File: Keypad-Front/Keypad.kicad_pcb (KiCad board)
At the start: 4 copper layers, 100.1 x 192.1 mm, 62 parts, among them J1 RTC STEMMA QT, J10 EXP QWIIC, J11 TOUCH QWIIC, J6 JST-PH 6, J7 JST-PH 6, J8 Feedback, U1 DS3231MZ, U2 LM1117-3.3, U3 CAP1214

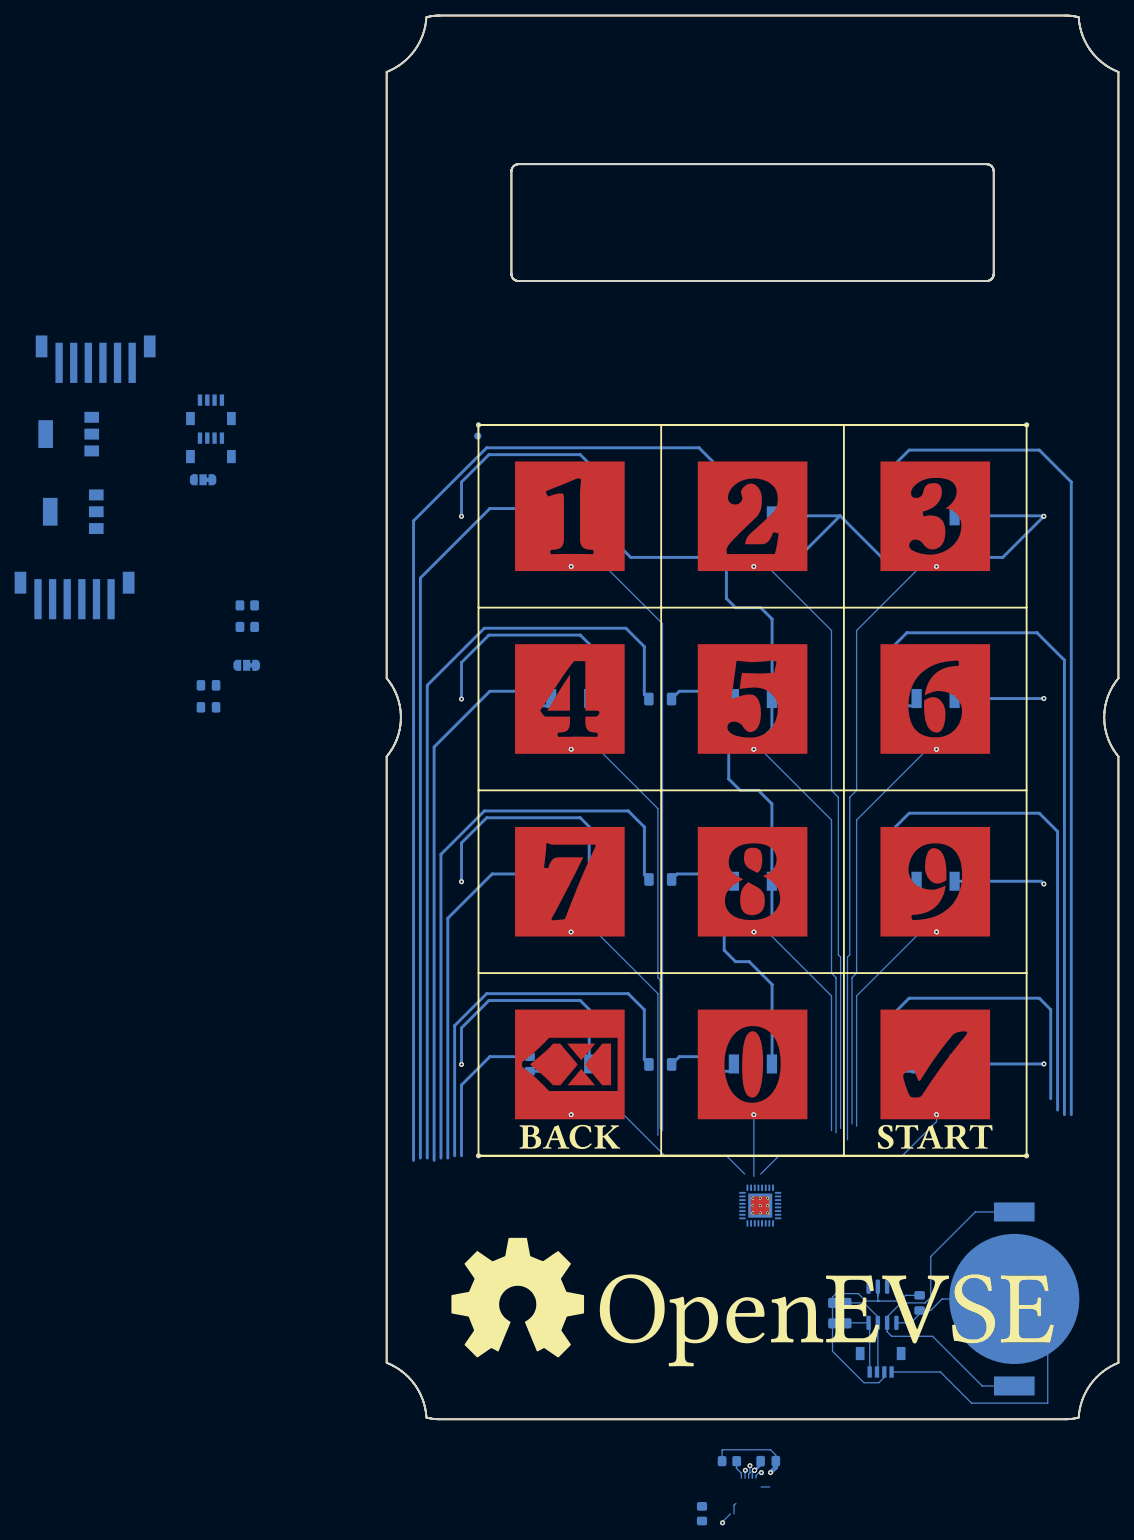
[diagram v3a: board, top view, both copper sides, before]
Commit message: Take 3, the JST-XH for the feedback is too large.
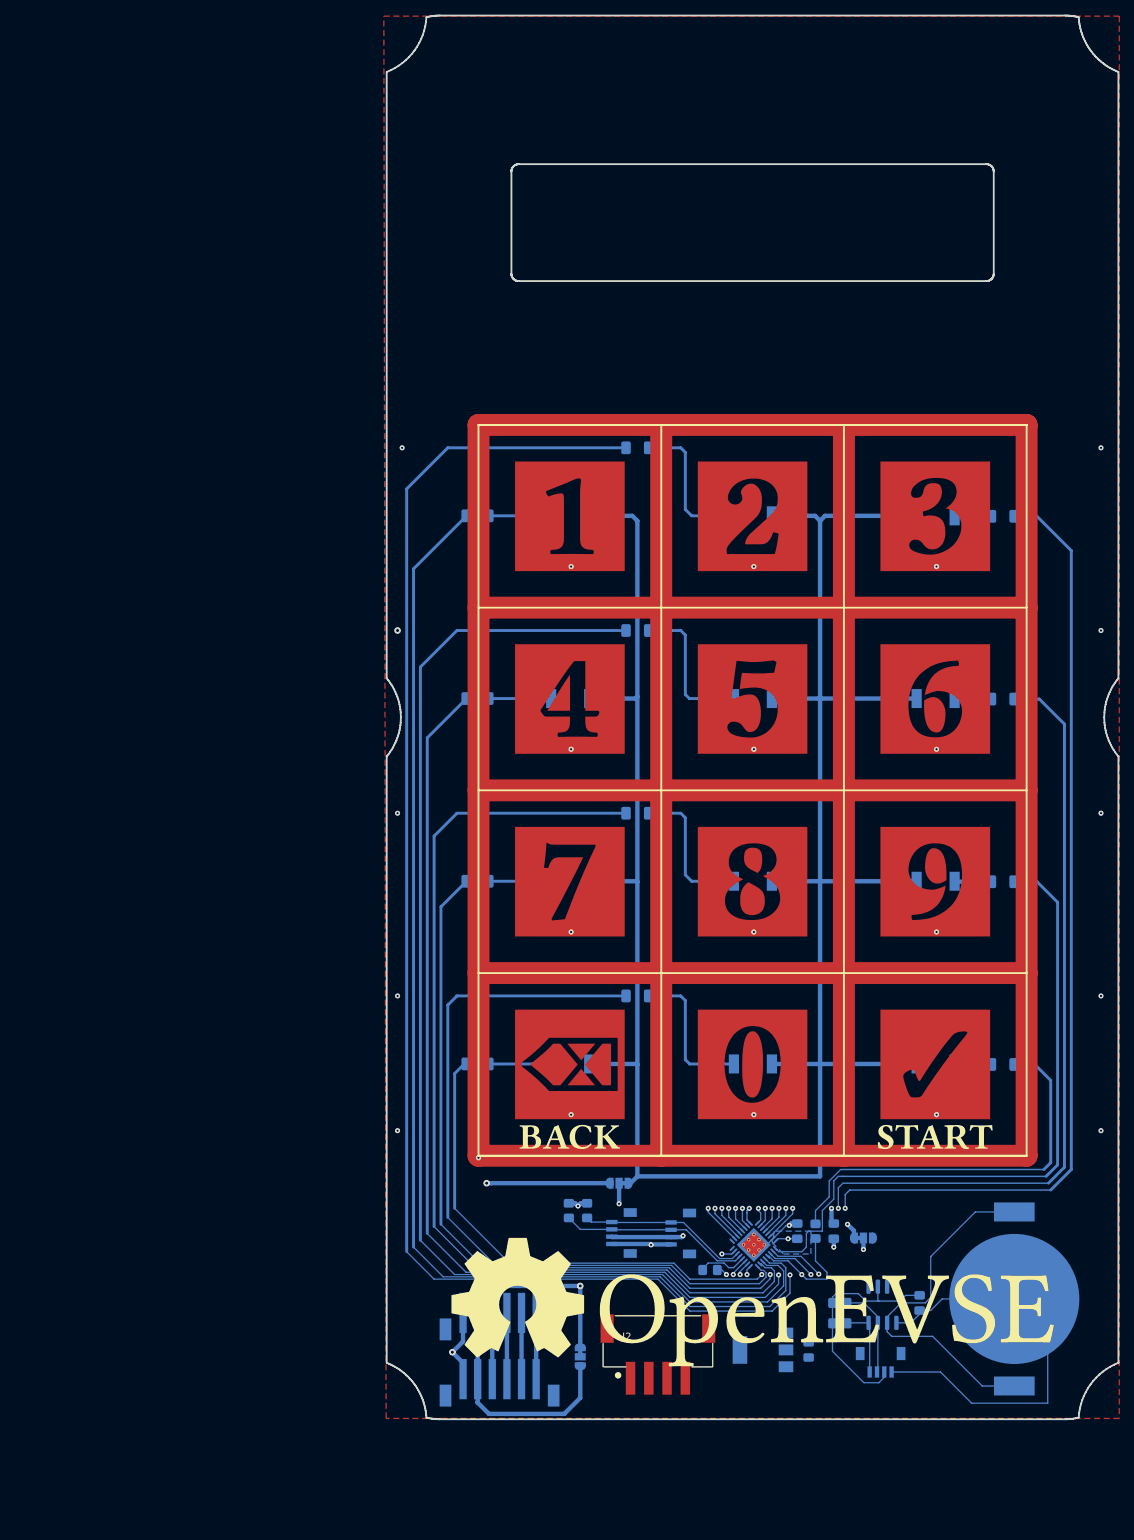
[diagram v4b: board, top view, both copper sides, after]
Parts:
- removed J8: Feedback, Package_TO_SOT_SMD:SOT-223-3_TabPin2
- removed R16, R20, R21: 0, Resistor_SMD:R_1206_3216Metric_Pad1.30x1.75mm_HandSolder
- added J2: JST-XH-4, Keypad:JST-XH-4-SMD, F.Cu at (91.2, 205.1)
- added JP3: PWR SEL, Jumper:SolderJumper-3_P1.3mm_Bridged12_RoundedPad1.0x1.5mm, B.Cu at (84.4, 202.2)
- R1, R10, R11, R12, R2, R3, R4, R5, R6, R7, R8, R9: footprint Resistor_SMD:R_0805_2012Metric_Pad1.20x1.40mm_HandSolder -> Resistor_SMD:R_1206_3216Metric_Pad1.30x1.75mm_HandSolder
- R17, R18: value 4.7k -> 10k
- TP14: moved to F.Cu
- moved U2 148.5 mm to (109.4, 201.2)
- moved J4 137.7 mm to (68.3, 196.2), turned to 0 degrees
- moved J6 130.3 mm to (96.8, 185.3), turned to -90 degrees
- moved J7 121.8 mm to (88.7, 185.3), turned to -90 degrees
- moved C3 120.3 mm to (115.6, 201.2), turned to 90 degrees
- moved J3 117.1 mm to (68.3, 205.2), turned to 0 degrees
- moved JP1 115.2 mm to (123.1, 185.9), turned to 0 degrees
- moved C2 113.6 mm to (119.1, 185.0), turned to 90 degrees
- moved JP2 111.8 mm to (89.7, 178.4)
- moved TP14 97.1 mm to (70.4, 173.3), turned to 0 degrees
- moved R17 95.0 mm to (85.3, 182.2), turned to -90 degrees
- moved R18 91.2 mm to (82.8, 182.2), turned to -90 degrees
- moved R15 41.7 mm to (116.6, 185.0)
- moved C4 31.7 mm to (114.1, 185.0), turned to 90 degrees
- moved R19 26.3 mm to (102.1, 190.3), turned to 0 degrees
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- renumbered J6 to J3, J7 to J4, J10 to J6, J11 to J7
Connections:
- net Net-(JP1-B) renamed /VREG
- R15 pad 1: /LED12 -> /LED10
- R15 pad 2: /LED10 -> /LED12
- R17 pad 2: Net-(U3-SMCLK) -> /TOUCH_SCL
- R18 pad 2: Net-(U3-SMDATA) -> /TOUCH_SDA
- U3 pad 1: /TOUCH_4 -> /TOUCH_11
- U3 pad 10: Net-(U3-LED2) -> /LED4
- U3 pad 11: /LED9 -> /LED7
- U3 pad 12: Net-(U3-LED4) -> /LED10
- U3 pad 13: /LED7 -> /LED1
- U3 pad 14: /LED6 -> /LED5
- U3 pad 15: Net-(U3-LED7) -> /LED8
- U3 pad 16: /LED4 -> /LED11
- U3 pad 17: /LED3 -> /LED2
- U3 pad 18: /LED2 -> /LED3
- U3 pad 19: /LED1 -> /LED6
- U3 pad 2: /TOUCH_3 -> /TOUCH_2
- U3 pad 21: Net-(U3-SMDATA) -> /TOUCH_SDA
- U3 pad 22: Net-(U3-SMCLK) -> /TOUCH_SCL
- U3 pad 27: /TOUCH_11 -> /TOUCH_4
- U3 pad 28: /TOUCH_9 -> /TOUCH_7
- U3 pad 29: /TOUCH_8 -> /TOUCH_10
- U3 pad 3: /TOUCH_2 -> /TOUCH_3
- U3 pad 30: /TOUCH_7 -> /TOUCH_1
- U3 pad 31: /TOUCH_6 -> /TOUCH_5
- U3 pad 32: /TOUCH_5 -> /TOUCH_8
- U3 pad 4: /TOUCH_1 -> /TOUCH_12
- U3 pad 5: /TOUCH_12 -> /TOUCH_9
- U3 pad 6: /TOUCH_10 -> /TOUCH_6
- U3 pad 9: /LED12 -> /LED9
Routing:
- net GND1: track 13.4 -> 1899.3 mm, vias 1 -> 15
- net /TOUCH_GUARD: track 252.8 -> 41.6 mm, vias 4 -> 2
- net /LED_VIN: track 507.3 -> 312.8 mm, vias 8 -> 0
- net /LED5: track 6.05 -> 168.2 mm
- net /LED8: track 5.91 -> 135.8 mm
- net Net-(U3-LED7): track 106.1 -> 0.00 mm
- net /LED11: track 6.04 -> 103.8 mm
- net Net-(U3-LED4): track 80.2 -> 0.00 mm
- net /DC_IN: track 0.00 -> 71.5 mm, vias 0 -> 2
- net /LED4: track 72.8 -> 144.2 mm, vias 0 -> 2
- net /LED10: track 20.6 -> 89.2 mm, vias 0 -> 2
- net /LED1: track 98.3 -> 164.6 mm
- net /LED7: track 46.5 -> 112.3 mm, vias 0 -> 2
- net /LED2: track 139.8 -> 204.1 mm, vias 0 -> 2
- net +3.3V: track 4.66 -> 59.4 mm, vias 3 -> 6
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- added copper zone on B.Cu, net +3.3V
- added copper zone on In1.Cu, net +3.3V
- added copper zone on F.Cu, net GND1
- added copper zone on In2.Cu, net GND1

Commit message: Complete!
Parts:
- removed J2: JST-XH-4, Keypad:JST-XH-4-SMD
- removed JP3: PWR SEL, Jumper:SolderJumper-3_P1.3mm_Bridged12_RoundedPad1.0x1.5mm
- added BZ1: Buzzer, Keypad:XDCR_SMT-1220-TW-R, B.Cu at (92.8, 200.6)
- added R16: 100, Resistor_SMD:R_1206_3216Metric_Pad1.30x1.75mm_HandSolder, B.Cu at (102.8, 198.8)
- added TP13: 5V, TestPoint:TestPoint_Pad_2.0x2.0mm, B.Cu at (62.5, 194.7)
- added TP15: 12V, TestPoint:TestPoint_Pad_2.0x2.0mm, B.Cu at (62.5, 199.7)
- TP1: value TestPoint -> KEY 1
- TP10: value TestPoint -> KEY BACK
- TP11: value TestPoint -> KEY 0
- TP12: value TestPoint -> KEY ENTER
- TP2: value TestPoint -> KEY 2
- TP3: value TestPoint -> KEY 3
- TP4: value TestPoint -> KEY 4
- TP5: value TestPoint -> KEY 5
- TP6: value TestPoint -> KEY 6
- TP7: value TestPoint -> KEY 7
- TP8: value TestPoint -> KEY 8
- TP9: value TestPoint -> KEY 9
- moved C3 12.3 mm to (103.8, 204.4), turned to -90 degrees
- moved U2 3.19 mm to (110.0, 204.4), turned to 0 degrees
- moved JP2 0.44 mm to (90.0, 178.8), turned to 90 degrees
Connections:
- JP2 pad 1: /LED_VIN -> +3.3V
- JP2 pad 2: +3.3V -> /LED_VIN
- U3 pad 24: /FEEDBACK -> Net-(U3-FEEDBACK)
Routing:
- net GND1: track 1899.3 -> 2021.0 mm, vias 15 -> 17
- net /DC_IN: track 71.5 -> 104.1 mm
- net /VREG: track 0.00 -> 31.4 mm
- net Net-(U3-FEEDBACK): track 0.00 -> 14.7 mm, vias 0 -> 2
- net /FEEDBACK: track 0.00 -> 12.5 mm
- net /12V_IN: track 32.2 -> 30.2 mm
- net /LED_VIN: track 312.8 -> 314.5 mm
- net +3.3V: track 59.4 -> 58.3 mm
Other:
- board text added: "+12V"
- board text added: "+3.3V"
- board text added: "+5V"
- board text added: "CSA 2023-07-07"
- board text added: "LED SUPPLY"
- board text added: "OPT REG"
- board text added: "OpenEVSE Keypad Add-On C. Scott Ananian"
- board text added: "Optional Power Tap"
- board text added: "RTC I2C"
- board text added: "STEMMA QT"

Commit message: First version of gerbers
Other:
- board text added: "JLCJLCJLCJLC"

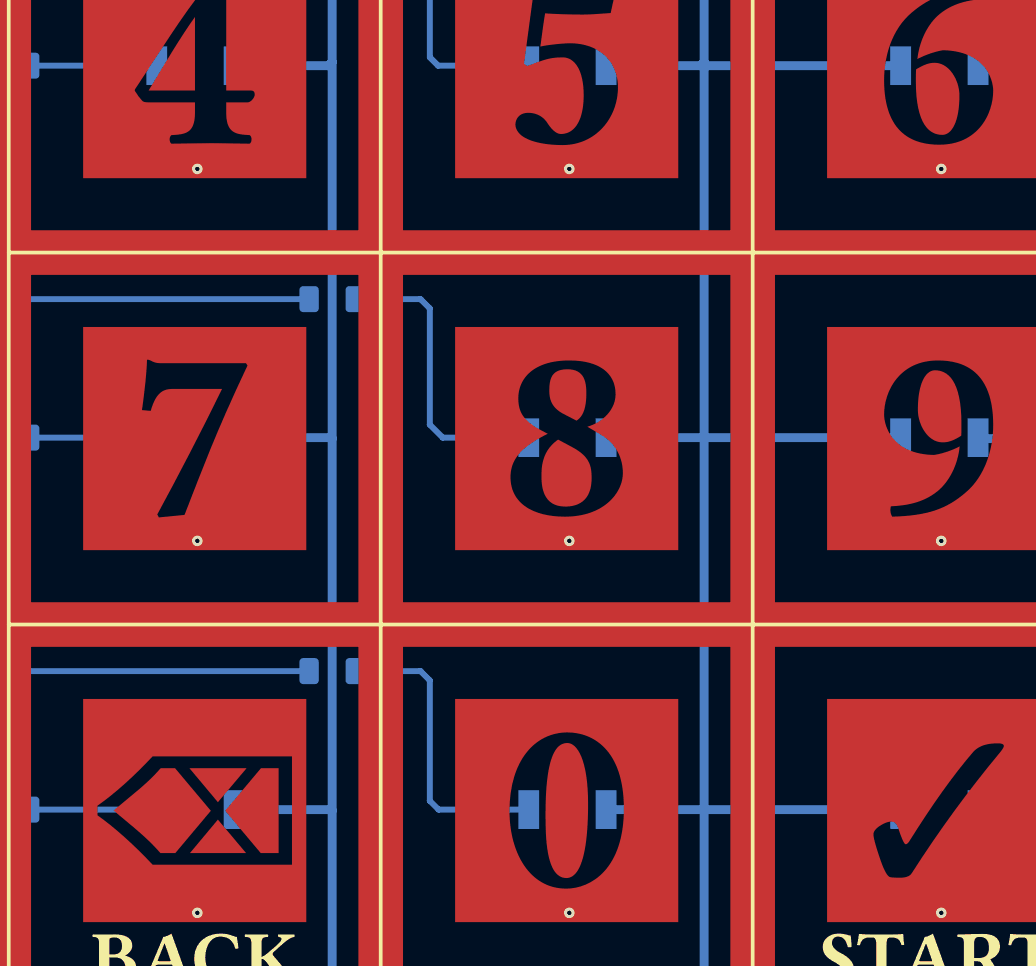
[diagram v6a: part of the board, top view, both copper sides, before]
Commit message: Second version, to fix the disconnected touch pad centers
Tried to get JLCPCB to adopt this, but apparently unsuccessfully.
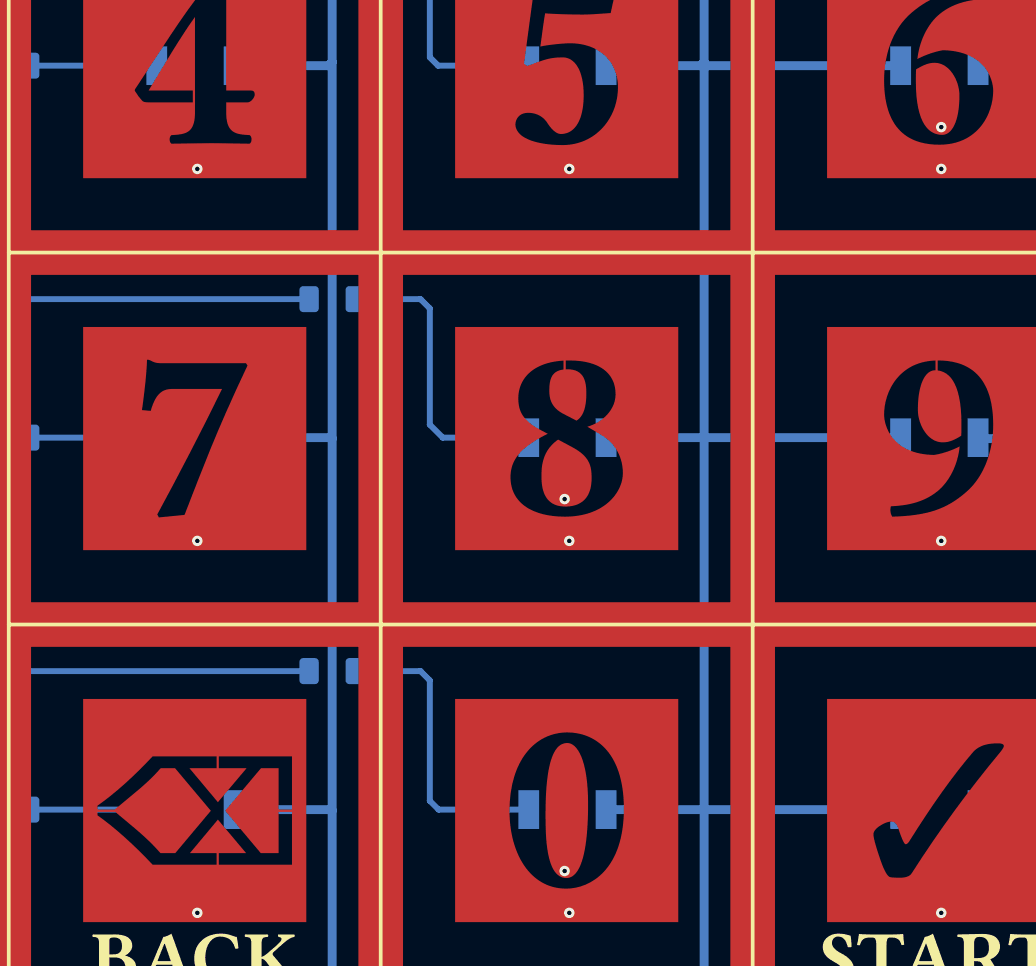
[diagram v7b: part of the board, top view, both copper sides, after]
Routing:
- net (no net): track 0.00 -> 11.9 mm
- net /TOUCH_8: track 47.9 -> 50.8 mm, vias 2 -> 3
- net /TOUCH_11: track 19.0 -> 22.0 mm, vias 2 -> 3
- net /TOUCH_6: track 100.0 -> 102.8 mm, vias 2 -> 3
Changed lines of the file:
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@@
     (effects (font (size 0.8 0.8) (thickness 0.15) bold) (justify bottom mirror))
   )
+  (segment (start 84.495563 164.934275) (end 84.495563 166.184275) (width 0.15) (layer "F.Cu") (net 0))
+  (segment (start 82.895173 113.782862) (end 82.895173 114.720362) (width 0.15) (layer "F.Cu") (net 0))
+  (segment (start 84.495563 159.621775) (end 84.495563 158.059275) (width 0.15) (layer "F.Cu") (net 0))
+  (segment (start 87.1875 162.1875) (end 90 162.1875) (width 0.15) (layer "F.Cu") (net 0))
+  (segment (start 132.8125 132.8125) (end 132.8125 131.5625) (width 0.15) (layer "F.Cu") (net 0))
+  (segment (start 107.8125 132.8125) (end 107.8125 131.5625) (width 0.15) (layer "F.Cu") (net 0))
+  (segment (start 78.75 162.1875) (end 75.9375 162.1875) (width 0.15) (layer "F.Cu") (net 0))
   (segment (start 110.598 112.122) (end 116.9405 112.122) (width 0.6) (layer "B.Cu") (net 1))
   (segment (start 85.598 87.122) (end 91.497 87.122) (width 0.6) (layer "B.Cu") (net 1))
@@
   (segment locked (start 133.125 119.0625) (end 131.601 119.0625) (width 0.15) (layer "F.Cu") (net 49))
   (via (at 113.4375 181.875) (size 0.7) (drill 0.3) (layers "F.Cu" "B.Cu") (net 49))
+  (via (at 133.125 116.25) (size 0.7) (drill 0.3) (layers "F.Cu" "B.Cu") (net 49))
   (via locked (at 133.125 119.0625) (size 0.7) (drill 0.3) (layers "F.Cu" "B.Cu") (net 49))
   (segment (start 142.1875 127.8125) (end 142.1875 148.4375) (width 0.15) (layer "In1.Cu") (net 49))
@@
   (segment (start 133.125 119.0625) (end 133.4375 119.0625) (width 0.15) (layer "In1.Cu") (net 49))
   (segment (start 115.9375 179.6875) (end 115.625 179.6875) (width 0.15) (layer "In1.Cu") (net 49))
+  (segment (start 133.125 119.0625) (end 133.125 116.25) (width 0.15) (layer "In1.Cu") (net 49))
   (segment (start 133.4375 119.0625) (end 142.1875 127.8125) (width 0.15) (layer "In1.Cu") (net 49))
   (segment (start 115.625 179.6875) (end 113.4375 181.875) (width 0.15) (layer "In1.Cu") (net 49))
@@
   (via (at 107.5 181.875) (size 0.7) (drill 0.3) (layers "F.Cu" "B.Cu") (net 51))
   (via locked (at 108.125 144.0625) (size 0.7) (drill 0.3) (layers "F.Cu" "B.Cu") (net 51))
+  (via (at 107.8125 141.25) (size 0.7) (drill 0.3) (layers "F.Cu" "B.Cu") (net 51))
   (segment (start 107.5 180) (end 107.5 181.875) (width 0.15) (layer "In1.Cu") (net 51))
+  (segment (start 108.125 144.0625) (end 107.8125 143.75) (width 0.15) (layer "In1.Cu") (net 51))
   (segment (start 100.3125 169.6875) (end 105 174.375) (width 0.15) (layer "In1.Cu") (net 51))
   (segment (start 105 177.5) (end 107.5 180) (width 0.15) (layer "In1.Cu") (net 51))
+  (segment (start 107.8125 143.75) (end 107.8125 141.25) (width 0.15) (layer "In1.Cu") (net 51))
   (segment (start 100.3125 151.875) (end 100.3125 169.6875) (width 0.15) (layer "In1.Cu") (net 51))
   (segment (start 105 174.375) (end 105 177.5) (width 0.15) (layer "In1.Cu") (net 51))
@@
   (segment (start 106.578204 184.974651) (end 104.6875 183.083947) (width 0.15) (layer "B.Cu") (net 53))
   (segment locked (start 108.125 169.0625) (end 106.601 169.0625) (width 0.15) (layer "F.Cu") (net 54))
+  (via (at 107.8125 166.25) (size 0.7) (drill 0.3) (layers "F.Cu" "B.Cu") (net 54))
   (via (at 108.75 181.875) (size 0.7) (drill 0.3) (layers "F.Cu" "B.Cu") (net 54))
   (via locked (at 108.125 169.0625) (size 0.7) (drill 0.3) (layers "F.Cu" "B.Cu") (net 54))
+  (segment (start 107.8125 168.75) (end 107.8125 166.25) (width 0.15) (layer "In1.Cu") (net 54))
   (segment (start 111.25 172.1875) (end 108.125 169.0625) (width 0.15) (layer "In1.Cu") (net 54))
+  (segment (start 108.125 169.0625) (end 107.8125 168.75) (width 0.15) (layer "In1.Cu") (net 54))
   (segment (start 111.25 176.5625) (end 111.25 172.1875) (width 0.15) (layer "In1.Cu") (net 54))
   (segment (start 108.75 181.875) (end 108.75 179.0625) (width 0.15) (layer "In1.Cu") (net 54))
